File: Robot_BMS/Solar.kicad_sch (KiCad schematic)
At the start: 22 parts, among them J4 691137710002, U2 LM3488MM, U3 CSD18563Q5A

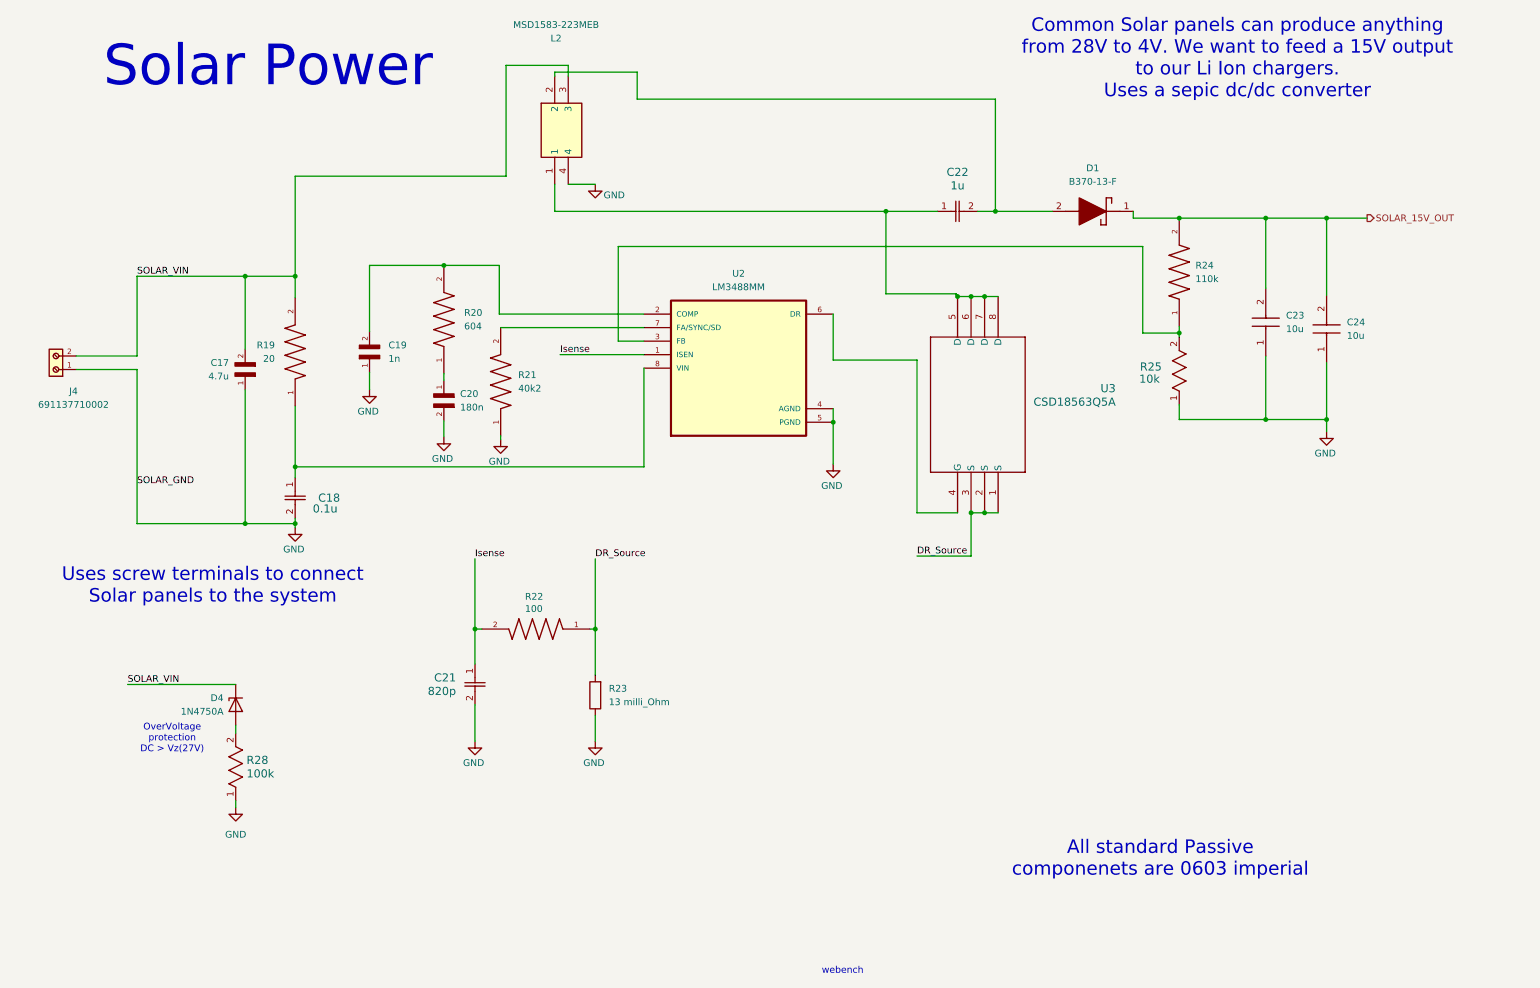
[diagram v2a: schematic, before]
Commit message: placed connectors for BMS PCB
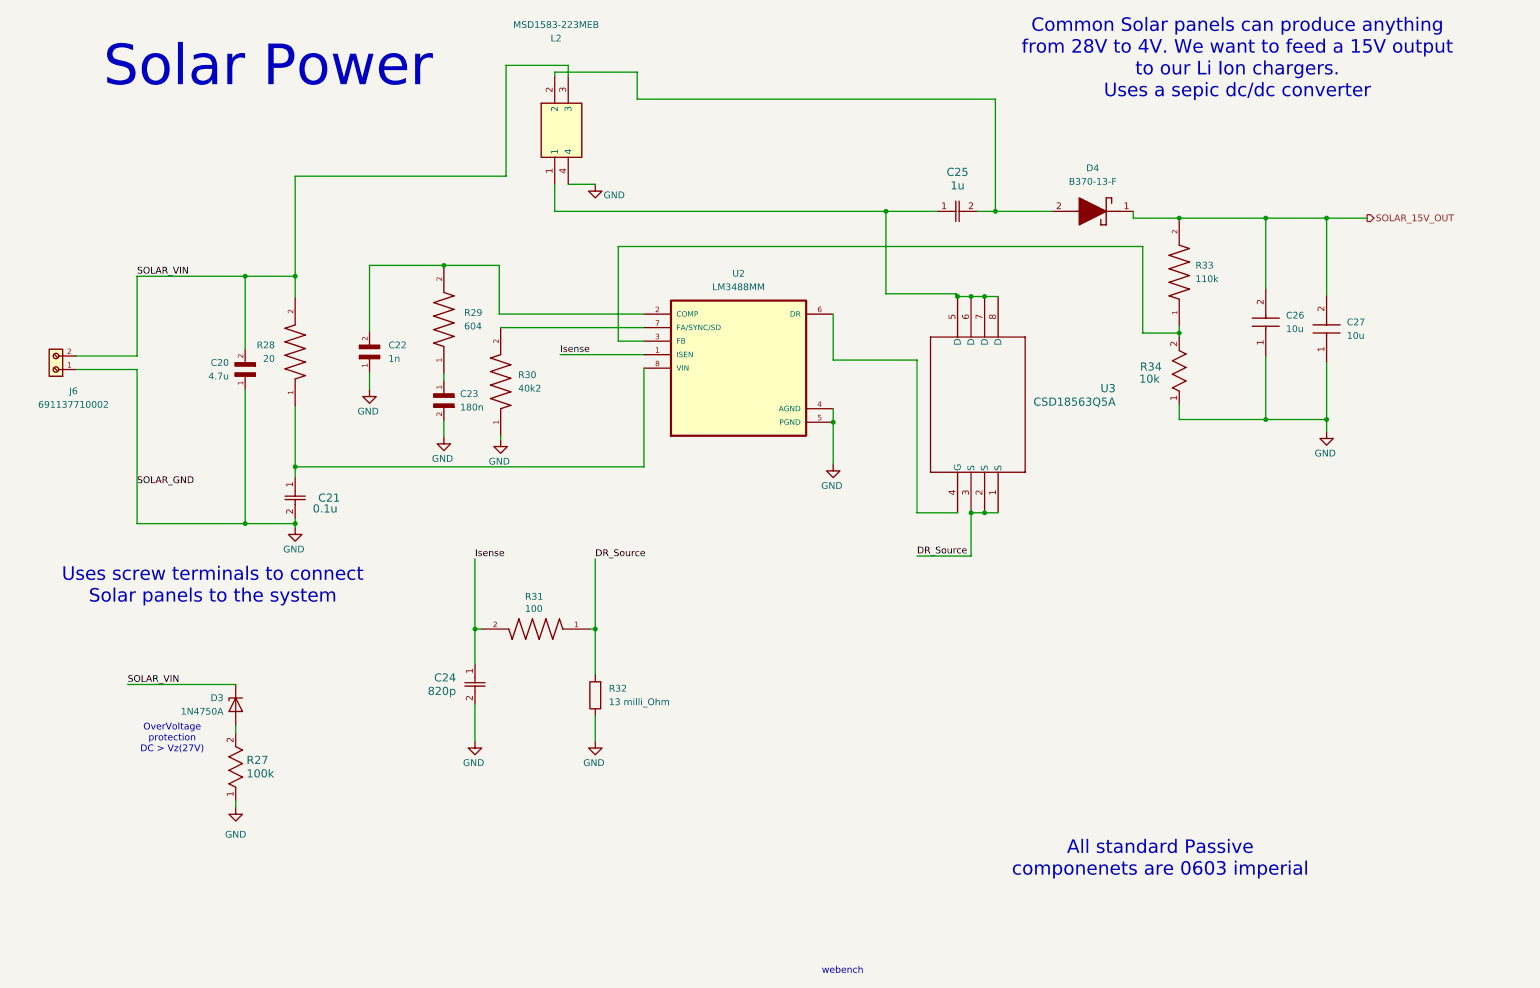
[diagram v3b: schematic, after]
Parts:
- renumbered C17 to C20, C18 to C21, C19 to C22, C20 to C23, C21 to C24, C22 to C25, C23 to C26, C24 to C27, D4 to D3, D1 to D4, J4 to J6, R28 to R27, R19 to R28, R20 to R29, R21 to R30, R22 to R31, R23 to R32, R24 to R33, R25 to R34
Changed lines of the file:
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@@
 		(dnp no)
 		(fields_autoplaced yes)
-		(property "Reference" "C24"
+		(property "Reference" "C27"
 			(at 258.064 72.6439 90)
 			(effects
@@
 			(project "Robot_BMS"
 				(path "/72551b1c-3d40-4199-8911-e5b015f4abec/ff8c01d9-7d3c-4161-8f4f-7a8402a9daec"
-					(reference "C24")
+					(reference "C27")
 					(unit 1)
 				)
@@
 		(on_board yes)
 		(dnp no)
-		(property "Reference" "#PWR030"
+		(property "Reference" "#PWR039"
 			(at 60.452 117.602 0)
 			(effects
@@
 			(project "Robot_BMS"
 				(path "/72551b1c-3d40-4199-8911-e5b015f4abec/ff8c01d9-7d3c-4161-8f4f-7a8402a9daec"
-					(reference "#PWR030")
+					(reference "#PWR039")
 					(unit 1)
 				)
@@
 		(dnp no)
 		(fields_autoplaced yes)
-		(property "Reference" "R28"
+		(property "Reference" "R27"
 			(at 51.308 154.9399 90)
 			(effects
@@
 			(project "Robot_BMS"
 				(path "/72551b1c-3d40-4199-8911-e5b015f4abec/ff8c01d9-7d3c-4161-8f4f-7a8402a9daec"
-					(reference "R28")
+					(reference "R27")
 					(unit 1)
 				)
@@
 		(on_board yes)
 		(dnp no)
-		(property "Reference" "C21"
+		(property "Reference" "C24"
 			(at 90.678 139.4459 90)
 			(effects
@@
 			(project ""
 				(path "/72551b1c-3d40-4199-8911-e5b015f4abec/ff8c01d9-7d3c-4161-8f4f-7a8402a9daec"
-					(reference "C21")
+					(reference "C24")
 					(unit 1)
 				)
@@
 		(on_board yes)
 		(dnp no)
-		(property "Reference" "#PWR037"
+		(property "Reference" "#PWR046"
 			(at 161.544 105.664 0)
 			(effects
@@
 			(project "Robot_BMS"
 				(path "/72551b1c-3d40-4199-8911-e5b015f4abec/ff8c01d9-7d3c-4161-8f4f-7a8402a9daec"
-					(reference "#PWR037")
+					(reference "#PWR046")
 					(unit 1)
 				)
@@
 		(on_board yes)
 		(dnp no)
-		(property "Reference" "D4"
+		(property "Reference" "D3"
 			(at 46.99 143.2559 90)
 			(effects
@@
 			(project "Robot_BMS"
 				(path "/72551b1c-3d40-4199-8911-e5b015f4abec/ff8c01d9-7d3c-4161-8f4f-7a8402a9daec"
-					(reference "D4")
+					(reference "D3")
 					(unit 1)
 				)
@@
 		(dnp no)
 		(fields_autoplaced yes)
-		(property "Reference" "D1"
+		(property "Reference" "D4"
 			(at 210.312 43.688 0)
 			(effects
@@
 			(project ""
 				(path "/72551b1c-3d40-4199-8911-e5b015f4abec/ff8c01d9-7d3c-4161-8f4f-7a8402a9daec"
-					(reference "D1")
+					(reference "D4")
 					(unit 1)
 				)
@@
 		(on_board yes)
 		(dnp no)
-		(property "Reference" "C18"
+		(property "Reference" "C21"
 			(at 64.77 105.664 90)
 			(effects
@@
 			(project "Robot_BMS"
 				(path "/72551b1c-3d40-4199-8911-e5b015f4abec/ff8c01d9-7d3c-4161-8f4f-7a8402a9daec"
-					(reference "C18")
+					(reference "C21")
 					(unit 1)
 				)
@@
 		(dnp no)
 		(fields_autoplaced yes)
-		(property "Reference" "C23"
+		(property "Reference" "C26"
 			(at 246.634 71.3739 90)
 			(effects
@@
 			(project "Robot_BMS"
 				(path "/72551b1c-3d40-4199-8911-e5b015f4abec/ff8c01d9-7d3c-4161-8f4f-7a8402a9daec"
-					(reference "C23")
+					(reference "C26")
 					(unit 1)
 				)
@@
 		(on_board yes)
 		(dnp no)
-		(property "Reference" "C17"
+		(property "Reference" "C20"
 			(at 48.006 80.2639 90)
 			(effects
@@
 			(project ""
 				(path "/72551b1c-3d40-4199-8911-e5b015f4abec/ff8c01d9-7d3c-4161-8f4f-7a8402a9daec"
-					(reference "C17")
+					(reference "C20")
 					(unit 1)
 				)
@@
 		(on_board yes)
 		(dnp no)
-		(property "Reference" "#PWR034"
+		(property "Reference" "#PWR043"
 			(at 99.06 101.092 0)
 			(effects
@@
 			(project "Robot_BMS"
 				(path "/72551b1c-3d40-4199-8911-e5b015f4abec/ff8c01d9-7d3c-4161-8f4f-7a8402a9daec"
-					(reference "#PWR034")
+					(reference "#PWR043")
 					(unit 1)
 				)
@@
 		(dnp no)
 		(fields_autoplaced yes)
-		(property "Reference" "#PWR041"
+		(property "Reference" "#PWR038"
 			(at 49.276 170.18 0)
 			(effects
@@
 			(project "Robot_BMS"
 				(path "/72551b1c-3d40-4199-8911-e5b015f4abec/ff8c01d9-7d3c-4161-8f4f-7a8402a9daec"
-					(reference "#PWR041")
+					(reference "#PWR038")
 					(unit 1)
 				)
@@
 		(dnp no)
 		(fields_autoplaced yes)
-		(property "Reference" "R23"
+		(property "Reference" "R32"
 			(at 119.38 141.4779 0)
 			(effects
@@
 			(project "Robot_BMS"
 				(path "/72551b1c-3d40-4199-8911-e5b015f4abec/ff8c01d9-7d3c-4161-8f4f-7a8402a9daec"
-					(reference "R23")
+					(reference "R32")
 					(unit 1)
 				)
@@
 		(on_board yes)
 		(dnp no)
-		(property "Reference" "R22"
+		(property "Reference" "R31"
 			(at 103.632 124.206 0)
 			(effects
@@
 			(project "Robot_BMS"
 				(path "/72551b1c-3d40-4199-8911-e5b015f4abec/ff8c01d9-7d3c-4161-8f4f-7a8402a9daec"
-					(reference "R22")
+					(reference "R31")
 					(unit 1)
 				)
@@
 		(on_board yes)
 		(dnp no)
-		(property "Reference" "#PWR038"
+		(property "Reference" "#PWR047"
 			(at 254.254 99.568 0)
 			(effects
@@
 			(project "Robot_BMS"
 				(path "/72551b1c-3d40-4199-8911-e5b015f4abec/ff8c01d9-7d3c-4161-8f4f-7a8402a9daec"
-					(reference "#PWR038")
+					(reference "#PWR047")
 					(unit 1)
 				)
@@
 		(dnp no)
 		(fields_autoplaced yes)
-		(property "Reference" "C19"
+		(property "Reference" "C22"
 			(at 77.978 76.9619 90)
 			(effects
@@
 			(project ""
 				(path "/72551b1c-3d40-4199-8911-e5b015f4abec/ff8c01d9-7d3c-4161-8f4f-7a8402a9daec"
-					(reference "C19")
+					(reference "C22")
 					(unit 1)
 				)
@@
 		(on_board yes)
 		(dnp no)
-		(property "Reference" "R25"
+		(property "Reference" "R34"
 			(at 221.234 81.026 90)
 			(effects
@@
 			(project "Robot_BMS"
 				(path "/72551b1c-3d40-4199-8911-e5b015f4abec/ff8c01d9-7d3c-4161-8f4f-7a8402a9daec"
-					(reference "R25")
+					(reference "R34")
 					(unit 1)
 				)
@@
 		(on_board yes)
 		(dnp no)
-		(property "Reference" "#PWR031"
+		(property "Reference" "#PWR040"
 			(at 74.422 91.694 0)
 			(effects
@@
 			(project "Robot_BMS"
 				(path "/72551b1c-3d40-4199-8911-e5b015f4abec/ff8c01d9-7d3c-4161-8f4f-7a8402a9daec"
-					(reference "#PWR031")
+					(reference "#PWR040")
 					(unit 1)
 				)
@@
 		(on_board yes)
 		(dnp no)
-		(property "Reference" "#PWR032"
+		(property "Reference" "#PWR041"
 			(at 88.392 100.584 0)
 			(effects
@@
 			(project "Robot_BMS"
 				(path "/72551b1c-3d40-4199-8911-e5b015f4abec/ff8c01d9-7d3c-4161-8f4f-7a8402a9daec"
-					(reference "#PWR032")
+					(reference "#PWR041")
 					(unit 1)
 				)
@@
 		(dnp no)
 		(fields_autoplaced yes)
-		(property "Reference" "R20"
+		(property "Reference" "R29"
 			(at 92.202 70.8659 90)
 			(effects
@@
 			(project ""
 				(path "/72551b1c-3d40-4199-8911-e5b015f4abec/ff8c01d9-7d3c-4161-8f4f-7a8402a9daec"
-					(reference "R20")
+					(reference "R29")
 					(unit 1)
 				)
@@
 		(on_board yes)
 		(dnp no)
-		(property "Reference" "J4"
+		(property "Reference" "J6"
 			(at 18.796 85.598 90)
 			(effects
@@
 			(project ""
 				(path "/72551b1c-3d40-4199-8911-e5b015f4abec/ff8c01d9-7d3c-4161-8f4f-7a8402a9daec"
-					(reference "J4")
+					(reference "J6")
 					(unit 1)
 				)
@@
 		(on_board yes)
 		(dnp no)
-		(property "Reference" "R19"
+		(property "Reference" "R28"
 			(at 56.642 76.9619 90)
 			(effects
@@
 			(project "Robot_BMS"
 				(path "/72551b1c-3d40-4199-8911-e5b015f4abec/ff8c01d9-7d3c-4161-8f4f-7a8402a9daec"
-					(reference "R19")
+					(reference "R28")
 					(unit 1)
 				)
@@
 		(on_board yes)
 		(dnp no)
-		(property "Reference" "R21"
+		(property "Reference" "R30"
 			(at 102.362 82.5499 90)
 			(effects
@@
 			(project ""
 				(path "/72551b1c-3d40-4199-8911-e5b015f4abec/ff8c01d9-7d3c-4161-8f4f-7a8402a9daec"
-					(reference "R21")
+					(reference "R30")
 					(unit 1)
 				)
@@
 		(on_board yes)
 		(dnp no)
-		(property "Reference" "#PWR035"
+		(property "Reference" "#PWR044"
 			(at 116.84 53.086 0)
 			(effects
@@
 			(project "Robot_BMS"
 				(path "/72551b1c-3d40-4199-8911-e5b015f4abec/ff8c01d9-7d3c-4161-8f4f-7a8402a9daec"
-					(reference "#PWR035")
+					(reference "#PWR044")
 					(unit 1)
 				)
@@
 		(on_board yes)
 		(dnp no)
-		(property "Reference" "#PWR036"
+		(property "Reference" "#PWR045"
 			(at 116.84 157.734 0)
 			(effects
@@
 			(project "Robot_BMS"
 				(path "/72551b1c-3d40-4199-8911-e5b015f4abec/ff8c01d9-7d3c-4161-8f4f-7a8402a9daec"
-					(reference "#PWR036")
+					(reference "#PWR045")
 					(unit 1)
 				)
@@
 		(dnp no)
 		(fields_autoplaced yes)
-		(property "Reference" "C20"
+		(property "Reference" "C23"
 			(at 91.44 86.1059 90)
 			(effects
@@
 			(project ""
 				(path "/72551b1c-3d40-4199-8911-e5b015f4abec/ff8c01d9-7d3c-4161-8f4f-7a8402a9daec"
-					(reference "C20")
+					(reference "C23")
 					(unit 1)
 				)
@@
 		(on_board yes)
 		(dnp no)
-		(property "Reference" "#PWR033"
+		(property "Reference" "#PWR042"
 			(at 94.234 157.734 0)
 			(effects
@@
 			(project "Robot_BMS"
 				(path "/72551b1c-3d40-4199-8911-e5b015f4abec/ff8c01d9-7d3c-4161-8f4f-7a8402a9daec"
-					(reference "#PWR033")
+					(reference "#PWR042")
 					(unit 1)
 				)
@@
 		(dnp no)
 		(fields_autoplaced yes)
-		(property "Reference" "C22"
+		(property "Reference" "C25"
 			(at 184.912 44.45 0)
 			(effects
@@
 			(project "Robot_BMS"
 				(path "/72551b1c-3d40-4199-8911-e5b015f4abec/ff8c01d9-7d3c-4161-8f4f-7a8402a9daec"
-					(reference "C22")
+					(reference "C25")
 					(unit 1)
 				)
@@
 		(on_board yes)
 		(dnp no)
-		(property "Reference" "R24"
+		(property "Reference" "R33"
 			(at 229.616 61.9759 90)
 			(effects
@@
 			(project ""
 				(path "/72551b1c-3d40-4199-8911-e5b015f4abec/ff8c01d9-7d3c-4161-8f4f-7a8402a9daec"
-					(reference "R24")
+					(reference "R33")
 					(unit 1)
 				)

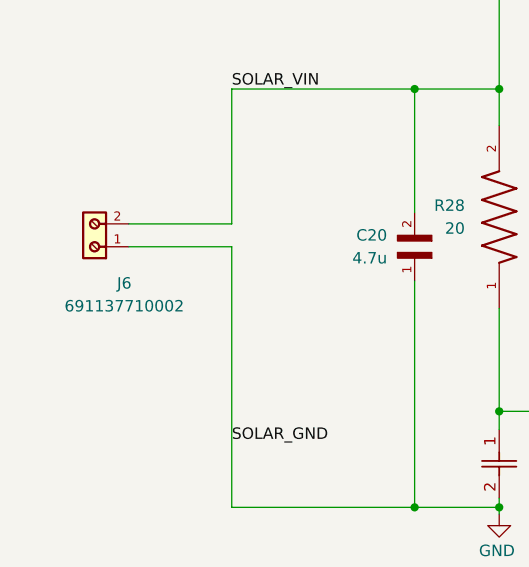
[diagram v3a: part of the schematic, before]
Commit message: creation of seperate 4 layer pcb for individual technical report
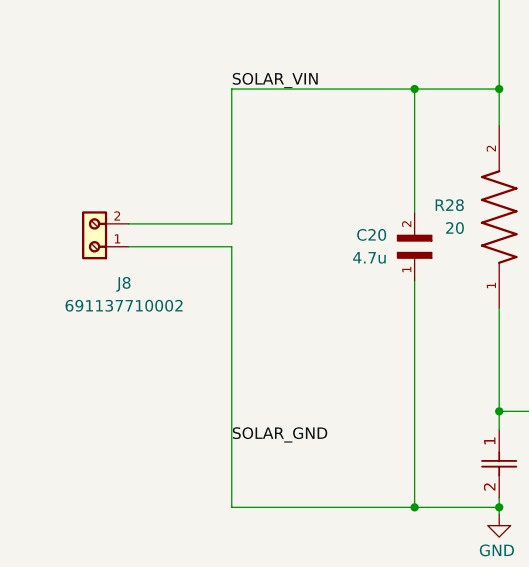
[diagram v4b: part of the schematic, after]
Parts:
- renumbered J6 to J8
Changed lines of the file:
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@@
 		(on_board yes)
 		(dnp no)
-		(property "Reference" "#PWR039"
+		(property "Reference" "#PWR040"
 			(at 60.452 117.602 0)
 			(effects
@@
 			(project "Robot_BMS"
 				(path "/72551b1c-3d40-4199-8911-e5b015f4abec/ff8c01d9-7d3c-4161-8f4f-7a8402a9daec"
-					(reference "#PWR039")
+					(reference "#PWR040")
 					(unit 1)
 				)
@@
 		(on_board yes)
 		(dnp no)
-		(property "Reference" "#PWR046"
+		(property "Reference" "#PWR047"
 			(at 161.544 105.664 0)
 			(effects
@@
 			(project "Robot_BMS"
 				(path "/72551b1c-3d40-4199-8911-e5b015f4abec/ff8c01d9-7d3c-4161-8f4f-7a8402a9daec"
-					(reference "#PWR046")
+					(reference "#PWR047")
 					(unit 1)
 				)
@@
 		(on_board yes)
 		(dnp no)
-		(property "Reference" "#PWR043"
+		(property "Reference" "#PWR044"
 			(at 99.06 101.092 0)
 			(effects
@@
 			(project "Robot_BMS"
 				(path "/72551b1c-3d40-4199-8911-e5b015f4abec/ff8c01d9-7d3c-4161-8f4f-7a8402a9daec"
-					(reference "#PWR043")
+					(reference "#PWR044")
 					(unit 1)
 				)
@@
 		(dnp no)
 		(fields_autoplaced yes)
-		(property "Reference" "#PWR038"
+		(property "Reference" "#PWR039"
 			(at 49.276 170.18 0)
 			(effects
@@
 			(project "Robot_BMS"
 				(path "/72551b1c-3d40-4199-8911-e5b015f4abec/ff8c01d9-7d3c-4161-8f4f-7a8402a9daec"
-					(reference "#PWR038")
+					(reference "#PWR039")
 					(unit 1)
 				)
@@
 		(on_board yes)
 		(dnp no)
-		(property "Reference" "#PWR047"
+		(property "Reference" "#PWR048"
 			(at 254.254 99.568 0)
 			(effects
@@
 			(project "Robot_BMS"
 				(path "/72551b1c-3d40-4199-8911-e5b015f4abec/ff8c01d9-7d3c-4161-8f4f-7a8402a9daec"
-					(reference "#PWR047")
+					(reference "#PWR048")
 					(unit 1)
 				)
@@
 		(on_board yes)
 		(dnp no)
-		(property "Reference" "#PWR040"
+		(property "Reference" "#PWR041"
 			(at 74.422 91.694 0)
 			(effects
@@
 			(project "Robot_BMS"
 				(path "/72551b1c-3d40-4199-8911-e5b015f4abec/ff8c01d9-7d3c-4161-8f4f-7a8402a9daec"
-					(reference "#PWR040")
+					(reference "#PWR041")
 					(unit 1)
 				)
@@
 		(on_board yes)
 		(dnp no)
-		(property "Reference" "#PWR041"
+		(property "Reference" "#PWR042"
 			(at 88.392 100.584 0)
 			(effects
@@
 			(project "Robot_BMS"
 				(path "/72551b1c-3d40-4199-8911-e5b015f4abec/ff8c01d9-7d3c-4161-8f4f-7a8402a9daec"
-					(reference "#PWR041")
+					(reference "#PWR042")
 					(unit 1)
 				)
@@
 		(on_board yes)
 		(dnp no)
-		(property "Reference" "J6"
+		(property "Reference" "J8"
 			(at 18.796 85.598 90)
 			(effects
@@
 			(project ""
 				(path "/72551b1c-3d40-4199-8911-e5b015f4abec/ff8c01d9-7d3c-4161-8f4f-7a8402a9daec"
-					(reference "J6")
+					(reference "J8")
 					(unit 1)
 				)
@@
 		(on_board yes)
 		(dnp no)
-		(property "Reference" "#PWR044"
+		(property "Reference" "#PWR045"
 			(at 116.84 53.086 0)
 			(effects
@@
 			(project "Robot_BMS"
 				(path "/72551b1c-3d40-4199-8911-e5b015f4abec/ff8c01d9-7d3c-4161-8f4f-7a8402a9daec"
-					(reference "#PWR044")
+					(reference "#PWR045")
 					(unit 1)
 				)
@@
 		(on_board yes)
 		(dnp no)
-		(property "Reference" "#PWR045"
+		(property "Reference" "#PWR046"
 			(at 116.84 157.734 0)
 			(effects
@@
 			(project "Robot_BMS"
 				(path "/72551b1c-3d40-4199-8911-e5b015f4abec/ff8c01d9-7d3c-4161-8f4f-7a8402a9daec"
-					(reference "#PWR045")
+					(reference "#PWR046")
 					(unit 1)
 				)
@@
 		(on_board yes)
 		(dnp no)
-		(property "Reference" "#PWR042"
+		(property "Reference" "#PWR043"
 			(at 94.234 157.734 0)
 			(effects
@@
 			(project "Robot_BMS"
 				(path "/72551b1c-3d40-4199-8911-e5b015f4abec/ff8c01d9-7d3c-4161-8f4f-7a8402a9daec"
-					(reference "#PWR042")
+					(reference "#PWR043")
 					(unit 1)
 				)

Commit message: halfway throgh battery management pcb layout
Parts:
- renumbered J8 to J9, R27 to R28, R28 to R29, R29 to R30, R30 to R31, R31 to R32, R32 to R33, R33 to R34, R34 to R35
